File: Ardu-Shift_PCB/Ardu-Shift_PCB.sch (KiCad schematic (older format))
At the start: 18 parts, among them U1 OLED(SPI), U2 Arduino_Pro_Micro, U3 SPDT_Slide

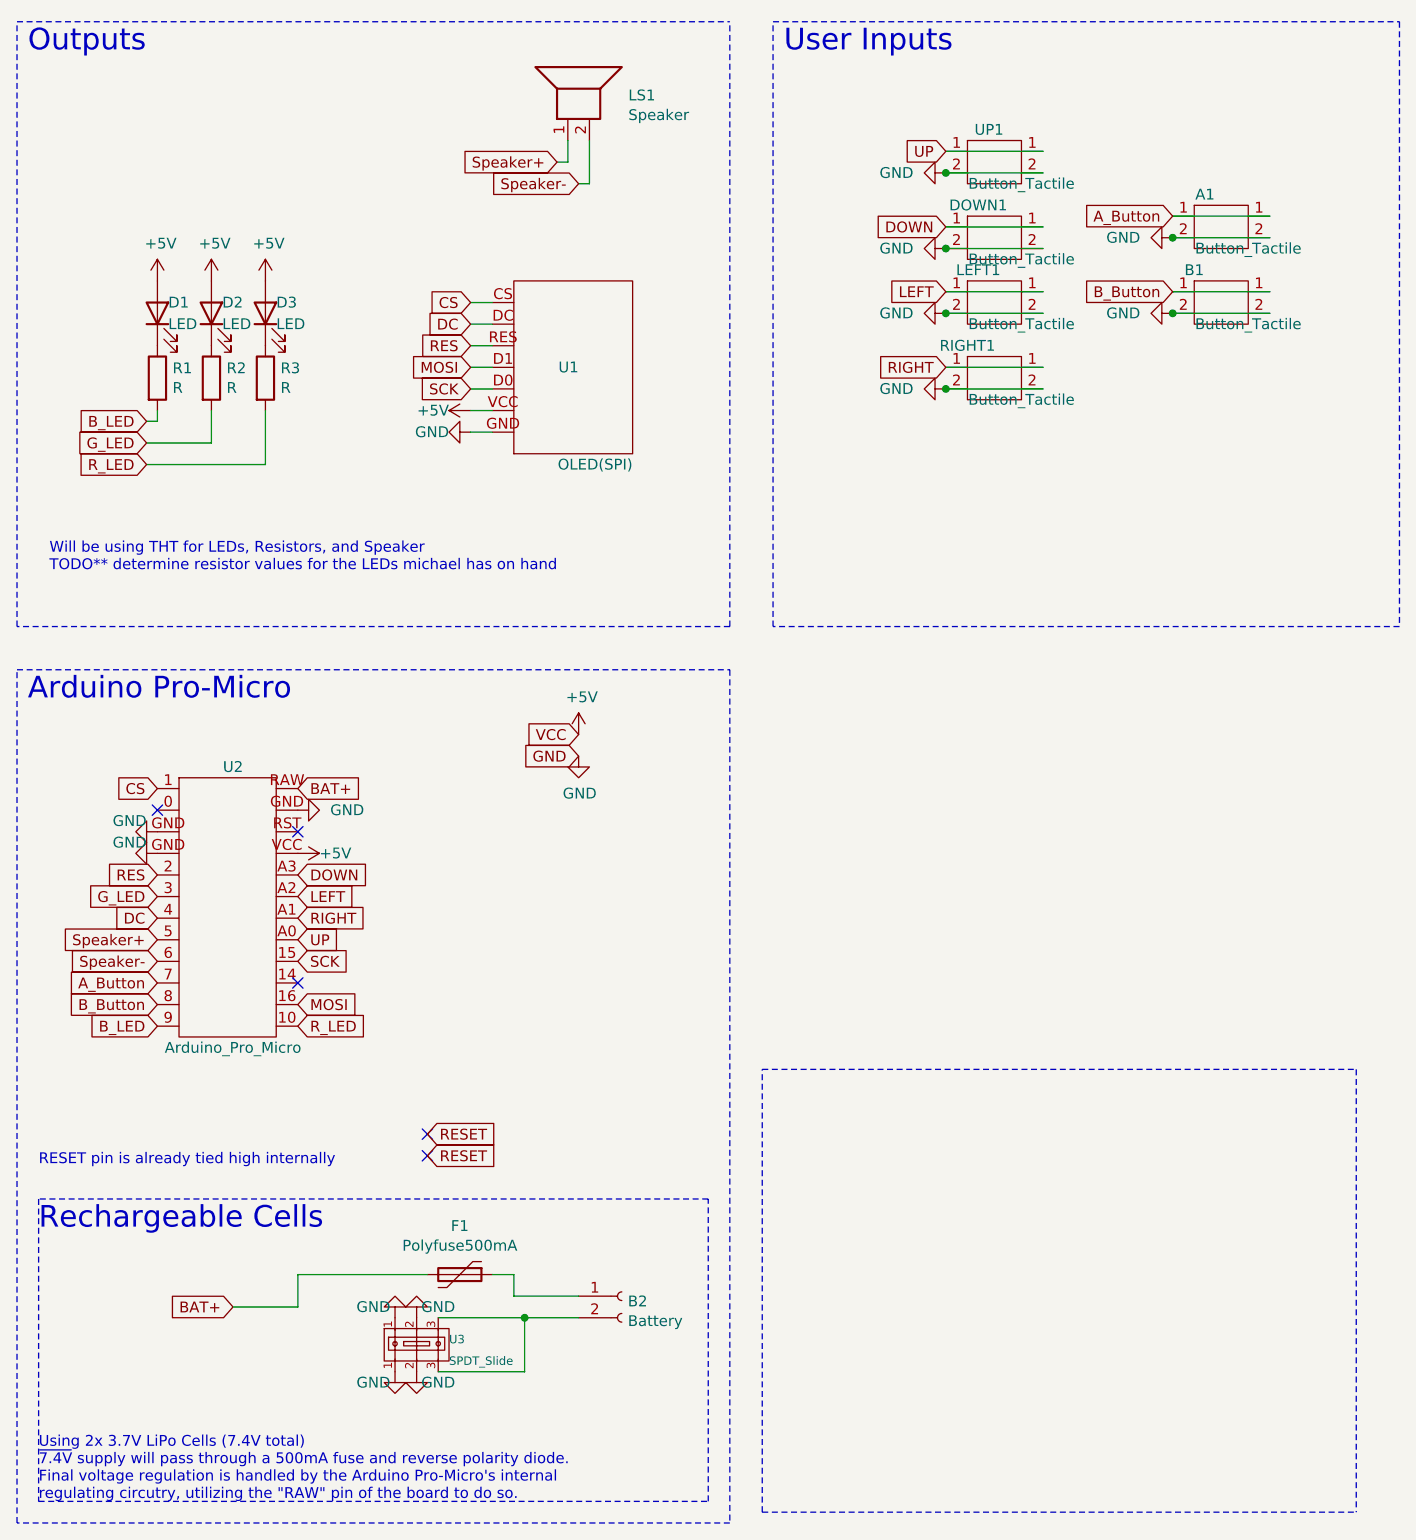
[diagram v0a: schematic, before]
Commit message: finalized PCB design - ready for final review by team members. Gerber files generated for manufacturing
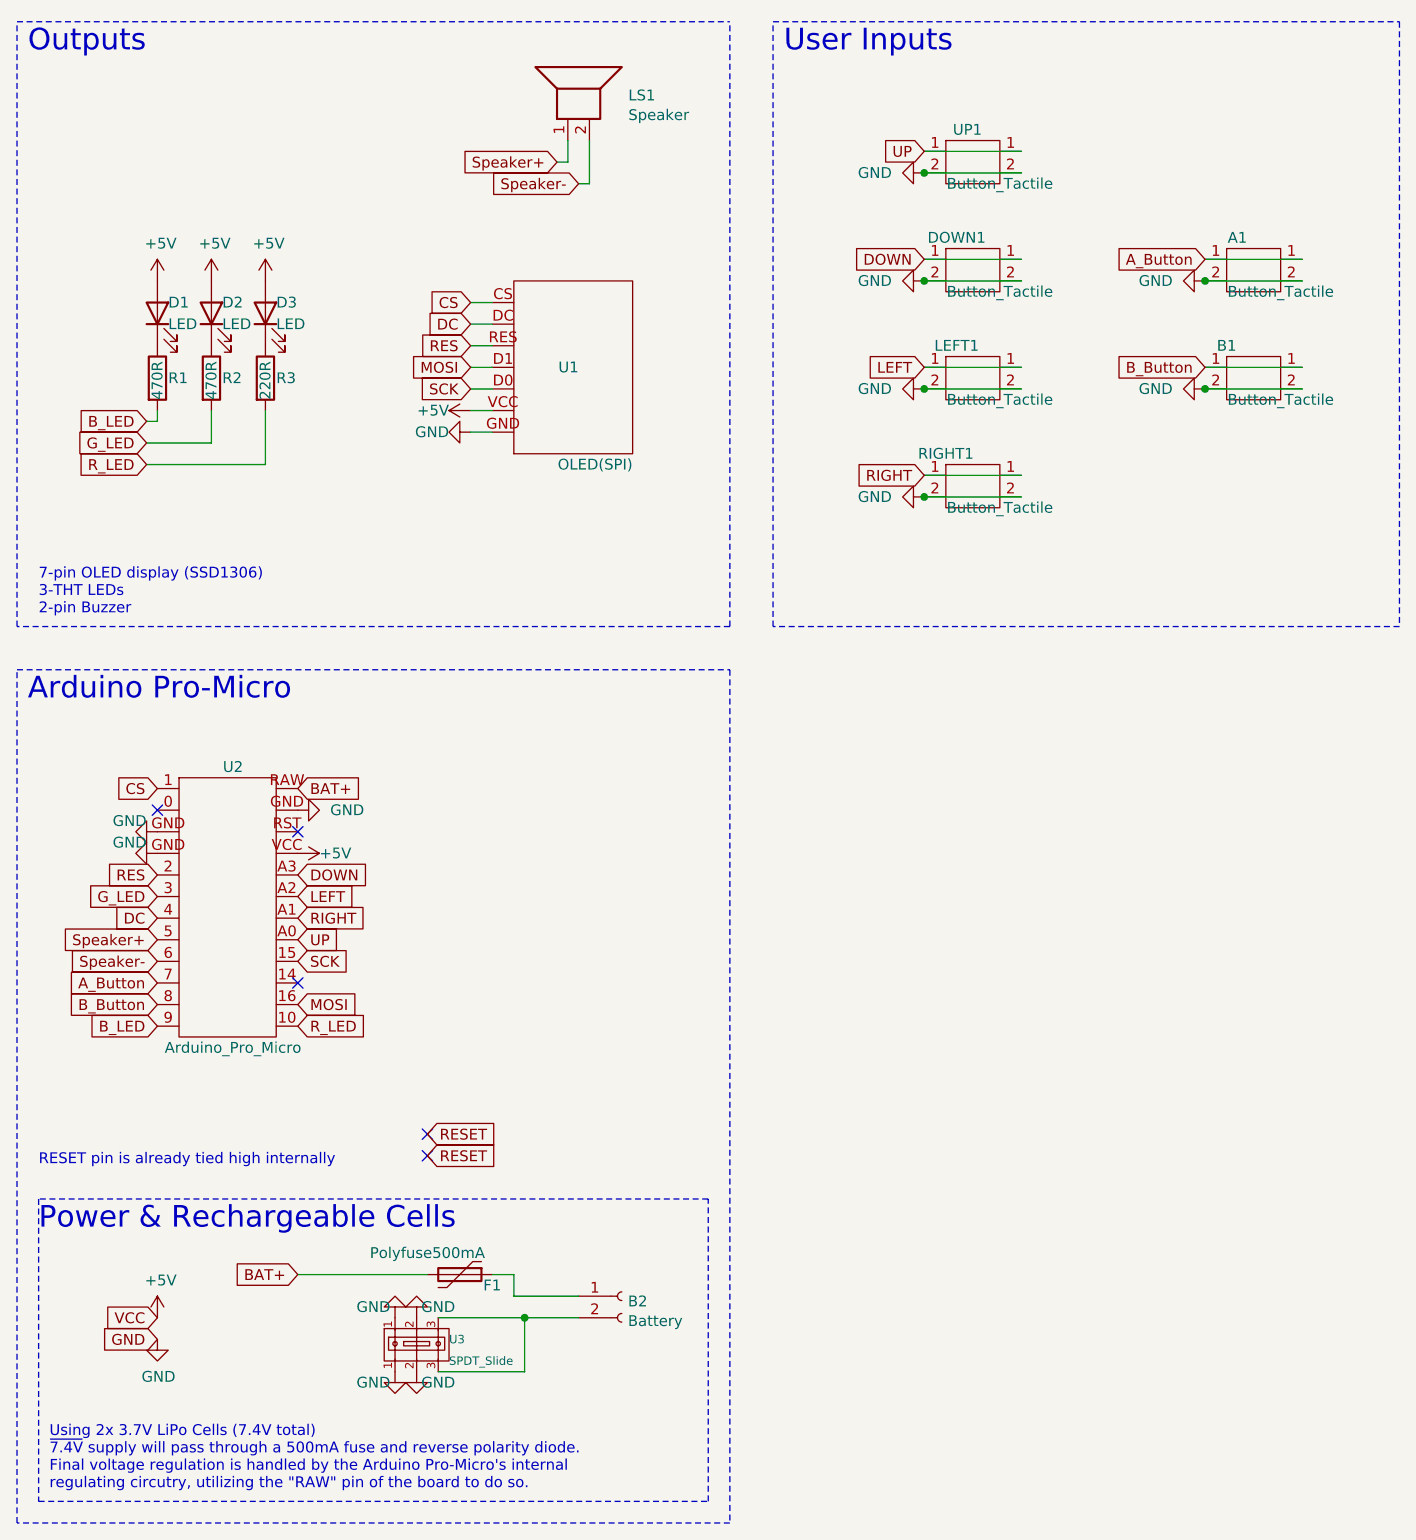
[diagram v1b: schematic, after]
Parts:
- R1, R2: value R -> 470R
- R3: value R -> 220R
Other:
- note added: "7-pin OLED display (SSD1306)\n3-THT LEDs \n2-pin Buzzer"
- note added: "Power & Rechargeable Cells\n"
- note removed: "Rechargeable Cells\n"
- note removed: "Will be using THT for LEDs, Resistors, and Speaker \nTODO** determine resistor values for the LEDs michael has on hand\n"
- moved on the sheet: A1, B1, DOWN1, LEFT1, RIGHT1, UP1
